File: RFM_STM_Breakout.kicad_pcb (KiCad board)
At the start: 2 copper layers, 29 parts, among them J1 USB_B_Micro, J2 Conn_01x02_Male, J3 Conn_01x16_Male, J4 Conn_01x12_Male, J5 Conn_01x15_Male, J6 Conn_Coaxial, SW1 SW_Push, U1 RFM95W-868S2, U2 XC6206P332MR, U3 STM32L053R8Tx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

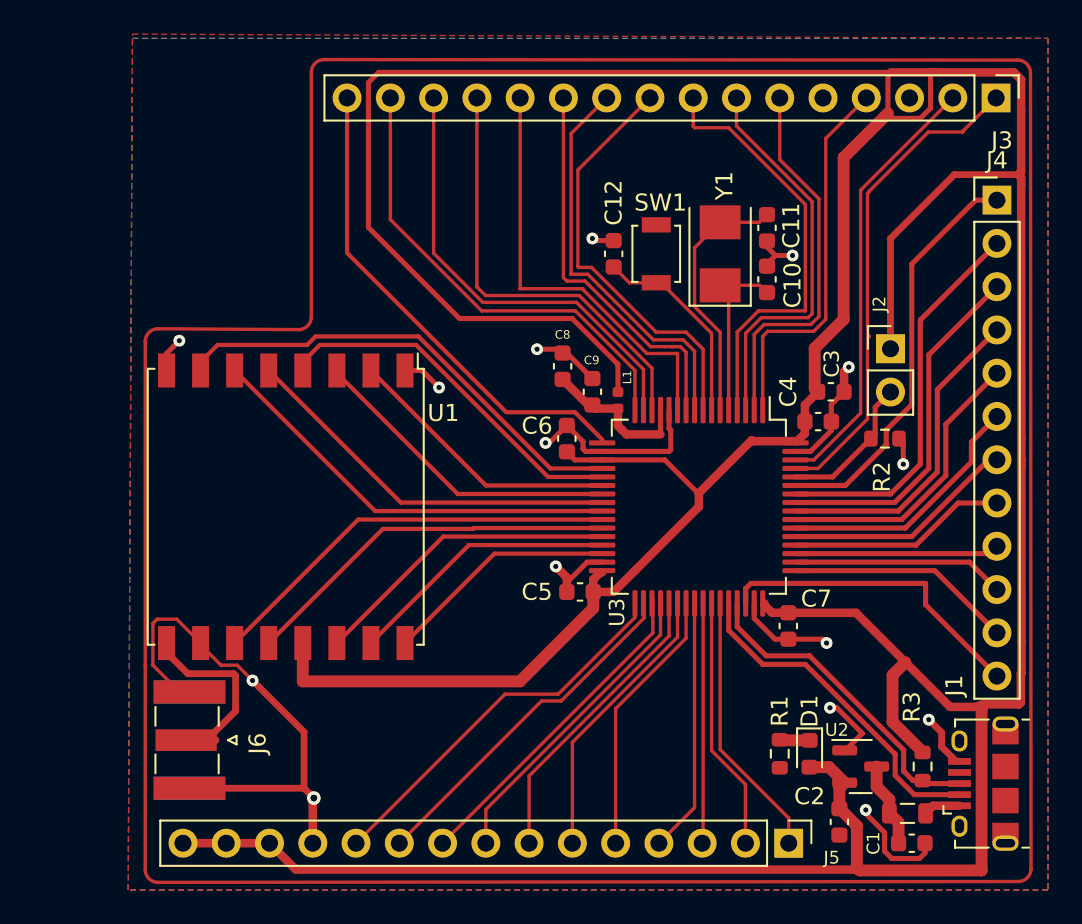
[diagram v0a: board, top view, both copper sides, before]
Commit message: Remove Top GND Layer
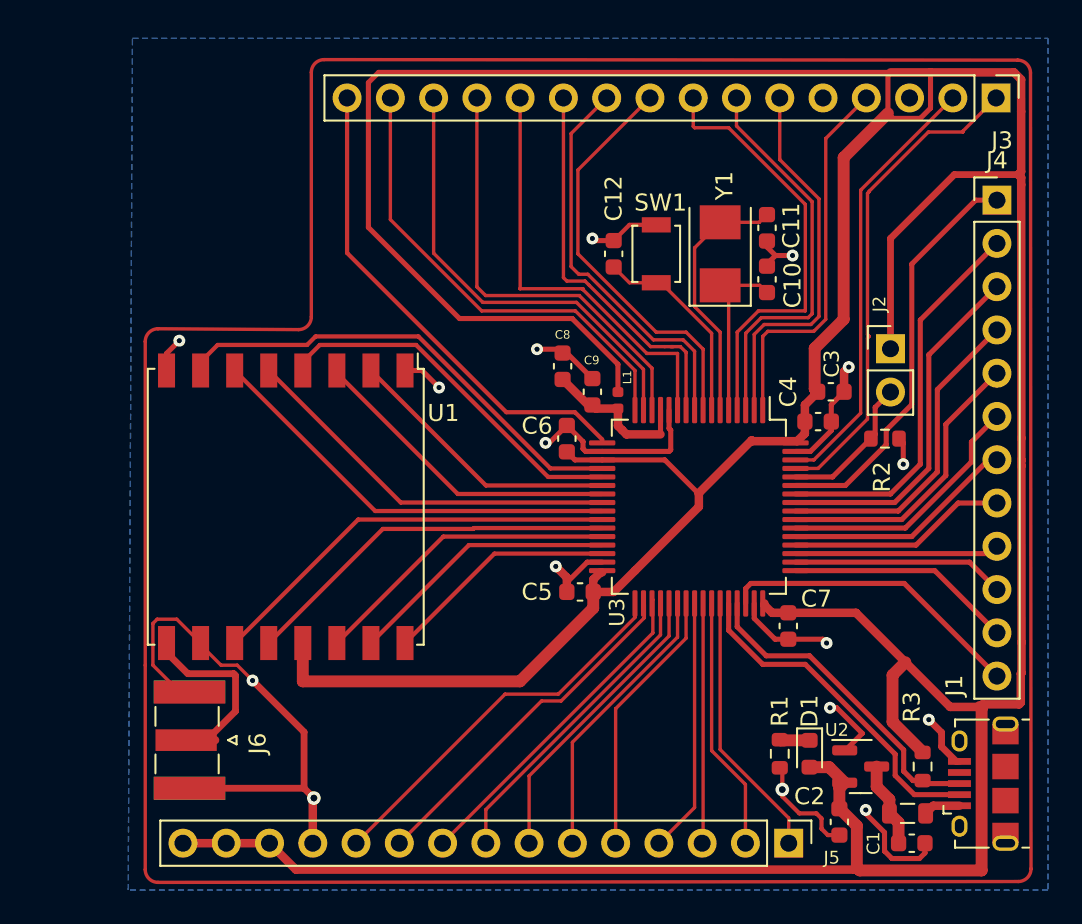
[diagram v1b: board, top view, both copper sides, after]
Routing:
- net GND: track 86.6 -> 95.9 mm, vias 15 -> 16
- net SWDIO: track 18.7 -> 18.0 mm
- removed copper zone on F.Cu, net GND
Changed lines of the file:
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@@
     (property "Sheetname" "")
     (attr smd)
-    (fp_text reference "C12" (at 3 0 90) (layer "F.SilkS")
+    (fp_text reference "C12" (at 3.25 0 90) (layer "F.SilkS")
       (effects (font (size 1 1) (thickness 0.15)))
     )
@@
   (segment (start 126.275 85.526041) (end 126.275 85) (width 0.3) (layer "F.Cu") (net 2))
   (segment (start 133.8 104.95) (end 133.612563 104.95) (width 0.4) (layer "F.Cu") (net 2))
+  (segment (start 126.075 109.275) (end 126.75 109.275) (width 0.25) (layer "F.Cu") (net 2))
   (segment (start 123 75.25) (end 122.5 75.75) (width 0.3) (layer "F.Cu") (net 2))
   (segment (start 92.3 100.2) (end 95.325 103.225) (width 0.4) (layer "F.Cu") (net 2))
@@
   (segment (start 121.75 96.551041) (end 122.973959 97.775) (width 0.3) (layer "F.Cu") (net 2))
   (segment (start 122.5 74.4) (end 122.5 74.75) (width 0.3) (layer "F.Cu") (net 2))
+  (segment (start 125.7 108.3) (end 125.7 108.9) (width 0.25) (layer "F.Cu") (net 2))
   (segment (start 89.25 98) (end 89.25 98.1) (width 0.2) (layer "F.Cu") (net 2))
+  (segment (start 123.4 105.475) (end 123.25 105.325) (width 0.25) (layer "F.Cu") (net 2))
   (segment (start 127.025 82.075) (end 127.3 81.8) (width 0.5) (layer "F.Cu") (net 2))
   (segment (start 95.325 103.225) (end 95.325 106.525) (width 0.4) (layer "F.Cu") (net 2))
   (segment (start 112.825 93.25) (end 111.948959 93.25) (width 0.3) (layer "F.Cu") (net 2))
   (segment (start 132.75 103.25) (end 132 102.5) (width 0.4) (layer "F.Cu") (net 2))
+  (segment (start 123.4 107) (end 124.4 108) (width 0.25) (layer "F.Cu") (net 2))
   (segment (start 89.25 98.1) (end 90.45 99.3) (width 0.2) (layer "F.Cu") (net 2))
   (segment (start 121.75 95.675) (end 121.75 96.551041) (width 0.3) (layer "F.Cu") (net 2))
@@
   (segment (start 122.5 75.75) (end 122.5 75.875) (width 0.3) (layer "F.Cu") (net 2))
   (segment (start 102.25 82) (end 103.25 83) (width 0.3) (layer "F.Cu") (net 2))
+  (segment (start 124.4 108) (end 125.4 108) (width 0.25) (layer "F.Cu") (net 2))
   (segment (start 124.175 86.75) (end 125.051041 86.75) (width 0.3) (layer "F.Cu") (net 2))
+  (segment (start 125.4 108) (end 125.7 108.3) (width 0.25) (layer "F.Cu") (net 2))
   (segment (start 86.45 99.3) (end 86.45 96.85) (width 0.2) (layer "F.Cu") (net 2))
+  (segment (start 113.5 74.375) (end 114.425 73.45) (width 0.25) (layer "F.Cu") (net 2))
   (segment (start 129.4 110.213173) (end 129.4 109.116834) (width 0.3) (layer "F.Cu") (net 2))
   (segment (start 110.75 94.15) (end 110.1 93.5) (width 0.5) (layer "F.Cu") (net 2))
   (segment (start 109.5 86.25) (end 109.725 86.25) (width 0.3) (layer "F.Cu") (net 2))
   (segment (start 128.096447 103.303553) (end 126.592894 101.8) (width 0.3) (layer "F.Cu") (net 2))
+  (segment (start 123.4 106.6) (end 123.4 107) (width 0.25) (layer "F.Cu") (net 2))
   (segment (start 127.1 104.3) (end 128.096447 103.303553) (width 0.3) (layer "F.Cu") (net 2))
   (segment (start 110.5 80.975) (end 110.75 80.975) (width 0.3) (layer "F.Cu") (net 2))
@@
   (segment (start 132.75 104.087437) (end 132.75 103.25) (width 0.4) (layer "F.Cu") (net 2))
   (segment (start 91.4 99.3) (end 92.3 100.2) (width 0.2) (layer "F.Cu") (net 2))
+  (segment (start 114.425 73.45) (end 116 73.45) (width 0.25) (layer "F.Cu") (net 2))
+  (segment (start 123.4 106.6) (end 123.4 105.475) (width 0.25) (layer "F.Cu") (net 2))
   (segment (start 127.025 83.25) (end 127.025 82.075) (width 0.5) (layer "F.Cu") (net 2))
   (segment (start 113.5 74.375) (end 112.375 74.375) (width 0.3) (layer "F.Cu") (net 2))
@@
   (segment (start 95.325 106.525) (end 95.9 107.1) (width 0.4) (layer "F.Cu") (net 2))
   (segment (start 111.7 86.6) (end 111.85 86.75) (width 0.3) (layer "F.Cu") (net 2))
+  (segment (start 125.7 108.9) (end 126.075 109.275) (width 0.25) (layer "F.Cu") (net 2))
   (segment (start 111.7 86.175) (end 111.7 86.6) (width 0.3) (layer "F.Cu") (net 2))
   (segment (start 126.275 85) (end 126.275 84) (width 0.3) (layer "F.Cu") (net 2))
@@
   (via (at 126.2 101.8) (size 0.7) (drill 0.3) (layers "F.Cu" "B.Cu") (free) (net 2))
   (via (at 110.1 93.5) (size 0.7) (drill 0.3) (layers "F.Cu" "B.Cu") (free) (net 2))
+  (via (at 123.4 106.6) (size 0.8) (drill 0.4) (layers "F.Cu" "B.Cu") (free) (net 2))
   (via (at 103.25 83) (size 0.7) (drill 0.3) (layers "F.Cu" "B.Cu") (free) (net 2))
   (via (at 127.3 81.8) (size 0.7) (drill 0.3) (layers "F.Cu" "B.Cu") (free) (net 2))
@@
   (segment (start 120.75 84.325) (end 120.75 79.75) (width 0.2) (layer "F.Cu") (net 20))
   (segment (start 118.17 67.67) (end 118.17 66) (width 0.2) (layer "F.Cu") (net 20))
-  (segment (start 111.45 75.95) (end 111.4 75.9) (width 0.2) (layer "F.Cu") (net 21))
-  (segment (start 111.4 70.23) (end 115.63 66) (width 0.2) (layer "F.Cu") (net 21))
-  (segment (start 118.75 84.325) (end 118.75 80.75) (width 0.2) (layer "F.Cu") (net 21))
-  (segment (start 117.75 79.75) (end 116 79.75) (width 0.2) (layer "F.Cu") (net 21))
-  (segment (start 112.2 75.95) (end 111.45 75.95) (width 0.2) (layer "F.Cu") (net 21))
-  (segment (start 118.75 80.75) (end 117.75 79.75) (width 0.2) (layer "F.Cu") (net 21))
-  (segment (start 111.4 75.9) (end 111.4 70.23) (width 0.2) (layer "F.Cu") (net 21))
-  (segment (start 116 79.75) (end 112.2 75.95) (width 0.2) (layer "F.Cu") (net 21))
-  (segment (start 111 68.09) (end 111 76.35) (width 0.2) (layer "F.Cu") (net 22))
+  (segment (start 117.75 79.75) (end 118.75 80.75) (width 0.2) (layer "F.Cu") (net 21))
+  (segment (start 111.4 75.15) (end 116 79.75) (width 0.2) (layer "F.Cu") (net 21))
+  (segment (start 115.63 66) (end 111.4 70.23) (width 0.2) (layer "F.Cu") (net 21))
+  (segment (start 116 79.75) (end 117.75 79.75) (width 0.2) (layer "F.Cu") (net 21))
+  (segment (start 111.4 70.23) (end 111.4 75.15) (width 0.2) (layer "F.Cu") (net 21))
+  (segment (start 118.75 80.75) (end 118.75 84.325) (width 0.2) (layer "F.Cu") (net 21))
+  (segment (start 111.45 76.35) (end 111.981371 76.35) (width 0.2) (layer "F.Cu") (net 22))
   (segment (start 118.25 80.86863) (end 118.25 84.325) (width 0.2) (layer "F.Cu") (net 22))
+  (segment (start 111.981371 76.35) (end 115.831371 80.2) (width 0.2) (layer "F.Cu") (net 22))
+  (segment (start 111 68.09) (end 111 75.9) (width 0.2) (layer "F.Cu") (net 22))
+  (segment (start 115.831371 80.2) (end 117.58137 80.2) (width 0.2) (layer "F.Cu") (net 22))
+  (segment (start 113.09 66) (end 111 68.09) (width 0.2) (layer "F.Cu") (net 22))
+  (segment (start 111 75.9) (end 111.45 76.35) (width 0.2) (layer "F.Cu") (net 22))
   (segment (start 117.58137 80.2) (end 118.25 80.86863) (width 0.2) (layer "F.Cu") (net 22))
-  (segment (start 111 76.35) (end 111.981371 76.35) (width 0.2) (layer "F.Cu") (net 22))
-  (segment (start 115.831371 80.2) (end 117.58137 80.2) (width 0.2) (layer "F.Cu") (net 22))
-  (segment (start 111.981371 76.35) (end 115.831371 80.2) (width 0.2) (layer "F.Cu") (net 22))
-  (segment (start 113.09 66) (end 111 68.09) (width 0.2) (layer "F.Cu") (net 22))
   (segment (start 112.032843 76.967158) (end 115.665685 80.6) (width 0.2) (layer "F.Cu") (net 23))
   (segment (start 117.75 80.934315) (end 117.415685 80.6) (width 0.2) (layer "F.Cu") (net 23))
@@
   (segment (start 123.775 108.275) (end 123.775 109.75) (width 0.2) (layer "F.Cu") (net 51))
   (segment (start 119.75 104.25) (end 123.775 108.275) (width 0.2) (layer "F.Cu") (net 51))
-  (segment (start 131.81 95.75) (end 131.81 94.5) (width 0.3) (layer "F.Cu") (net 52))
-  (segment (start 136 99.94) (end 131.81 95.75) (width 0.3) (layer "F.Cu") (net 52))
+  (segment (start 130.56 94.5) (end 136 99.94) (width 0.3) (layer "F.Cu") (net 52))
+  (segment (start 121.25 94.798959) (end 121.548959 94.5) (width 0.3) (layer "F.Cu") (net 52))
+  (segment (start 121.548959 94.5) (end 130.56 94.5) (width 0.3) (layer "F.Cu") (net 52))
   (segment (start 121.25 95.675) (end 121.25 94.798959) (width 0.3) (layer "F.Cu") (net 52))
-  (segment (start 121.25 94.798959) (end 121.548959 94.5) (width 0.3) (layer "F.Cu") (net 52))
-  (segment (start 121.548959 94.5) (end 131.81 94.5) (width 0.3) (layer "F.Cu") (net 52))
   (segment (start 136 97.4) (end 132.35 93.75) (width 0.3) (layer "F.Cu") (net 53))
   (segment (start 132.35 93.75) (end 124.175 93.75) (width 0.3) (layer "F.Cu") (net 53))
@@
   (segment (start 124.175 88.75) (end 127.102817 88.75) (width 0.3) (layer "F.Cu") (net 63))
   (segment (start 131 83.997183) (end 131 75.75) (width 0.3) (layer "F.Cu") (net 63))
-  (zone (net 2) (net_name "GND") (layer "F.Cu") (hatch edge 0.508)
-    (connect_pads (clearance 0.508))
-    (min_thickness 0.254) (filled_areas_thickness no)
-    (fill yes (thermal_gap 0.508) (thermal_bridge_width 0.508))
-    (polygon
-      (pts
-        (xy 139 62.5)
-        (xy 139 112.5)
-        (xy 85 112.5)
-        (xy 85.25 62.25)
-      )
-    )
-  )
   (zone (net 2) (net_name "GND") (layer "B.Cu") (hatch edge 0.508)
     (connect_pads (clearance 0.508))

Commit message: Change angles and 3.3V Rail
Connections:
- J5 pad 12: GND -> +3.3V
- J5 pad 15: +3.3V -> GND
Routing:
- net GND: track 95.9 -> 84.7 mm
- net +3.3V: track 286.2 -> 294.8 mm
- net Net-(J6-Pad1): track 13.5 -> 11.7 mm
- net PC3: track 25.4 -> 24.1 mm

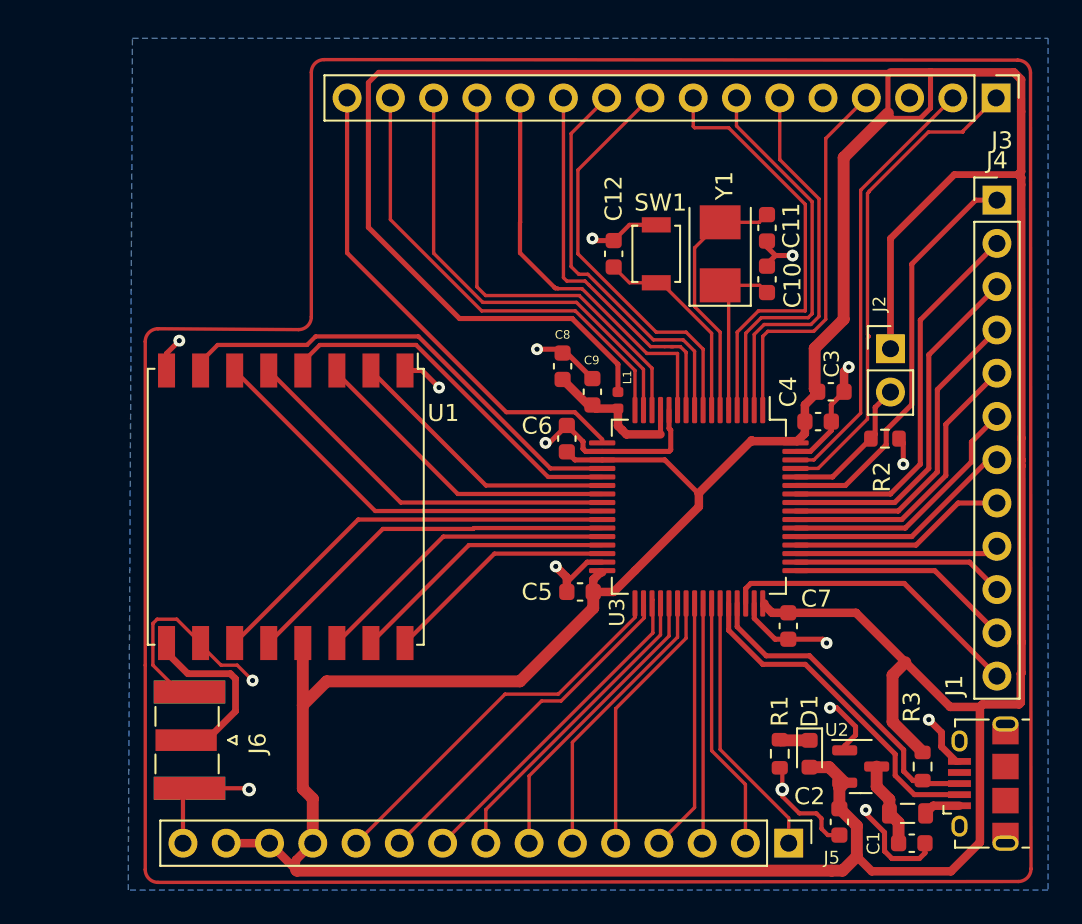
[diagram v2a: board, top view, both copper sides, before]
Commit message: impedance adjustment of the signal trace, improve GND conncetion, fix board border
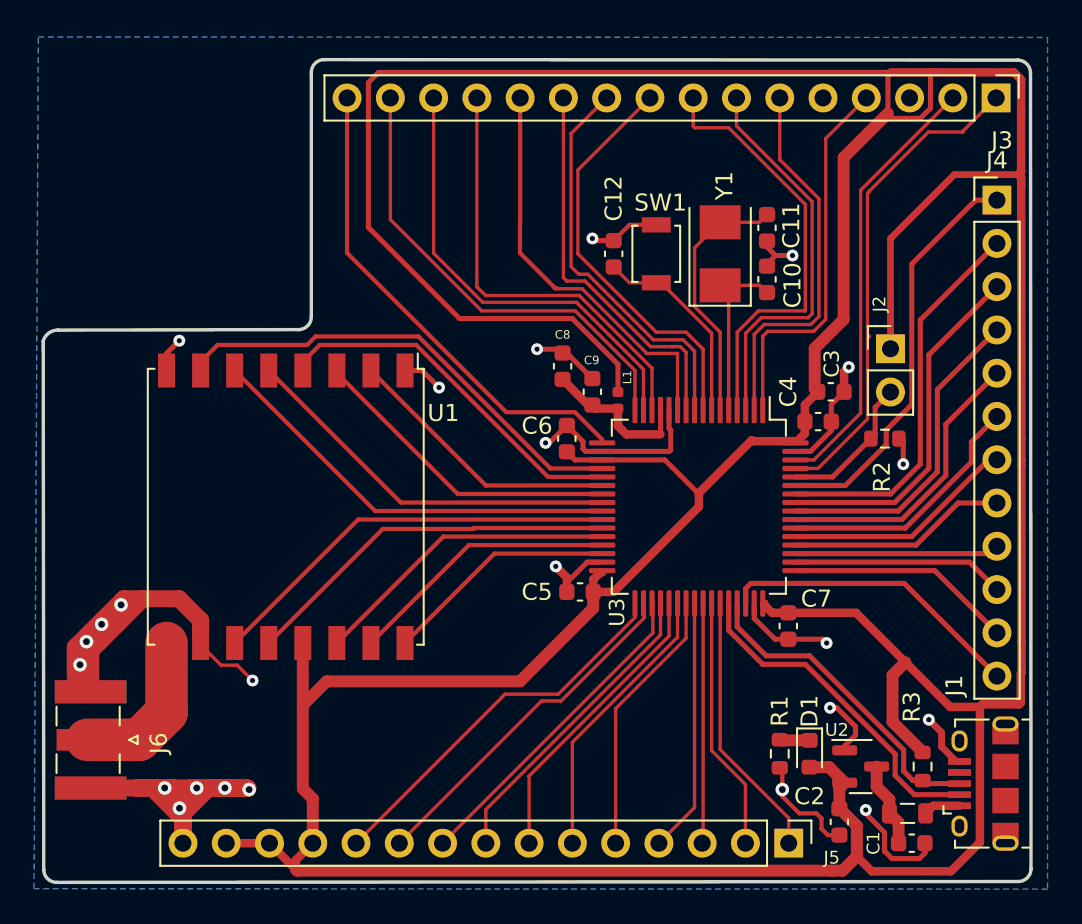
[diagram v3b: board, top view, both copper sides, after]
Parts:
- moved J6 5.81 mm to (82.8, 103.7)
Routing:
- net GND: track 84.7 -> 116.8 mm, vias 16 -> 24
- net Net-(J6-Pad1): track 11.7 -> 9.40 mm
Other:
- board outline added: 58 x 48.3 mm
